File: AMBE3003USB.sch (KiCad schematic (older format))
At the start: 18 parts, among them P1 USB_B, U1 FT232RL, U2 TPS78319, U3 LD1117S33TR

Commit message: Add AMBE3003 chip to schematic
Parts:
- added C10, C9: 24p, symbol C
- added JP?: JUMPER, symbol JUMPER
- added U?: AMBE3003, symbol AMBE3003
- added Y1: 29.4912, symbol Crystal
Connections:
- wire segments 60 -> 117
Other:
- moved on the sheet: C1, C2, C3, C4, C5, C6, C7, C8, R1, R2, R3, U1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

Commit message: Add jumpers for AMBE3003 and some refactoring
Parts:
- removed JP?: JUMPER, symbol JUMPER
- added P2: CONN_02X16, symbol CONN_02X16
- added R10, R11, R12, R13, R14, R15, R16, R17, R18, R19, R4, R5, R6, R7, R8, R9: 3k3, symbol R
- gave numbers to parts that had none: 1
- renumbered U1 to U2, U2 to U3, U3 to U4
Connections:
- wire segments 117 -> 195
- no-connect marks 13 -> 40
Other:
- moved on the sheet: C1, C10, C2, C3, C4, C9, R3, U1

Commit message: Add Rs and Cs to USB connection
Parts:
- added C11, C12: 47p, symbol C
- added R20, R21: 27, symbol R
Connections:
- wire segments 195 -> 203
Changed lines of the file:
@@
 L USB_B P1
 U 1 1 591BECF9
-P 6200 4450
-F 0 "P1" H 6400 4250 50  0000 C CNN
-F 1 "USB_B" H 6150 4650 50  0000 C CNN
-F 2 "" V 6150 4350 50  0001 C CNN
-F 3 "" V 6150 4350 50  0000 C CNN
-	1    6200 4450
+P 5850 4450
+F 0 "P1" H 6050 4250 50  0000 C CNN
+F 1 "USB_B" H 5800 4650 50  0000 C CNN
+F 2 "" V 5800 4350 50  0001 C CNN
+F 3 "" V 5800 4350 50  0000 C CNN
+	1    5850 4450
 	0    -1   1    0
 $EndComp
@@
 L GND #PWR02
 U 1 1 591BEEC2
-P 6550 5000
-F 0 "#PWR02" H 6550 4750 50  0001 C CNN
-F 1 "GND" H 6550 4850 50  0000 C CNN
-F 2 "" H 6550 5000 50  0000 C CNN
-F 3 "" H 6550 5000 50  0000 C CNN
-	1    6550 5000
+P 6700 4950
+F 0 "#PWR02" H 6700 4700 50  0001 C CNN
+F 1 "GND" H 6700 4800 50  0000 C CNN
+F 2 "" H 6700 4950 50  0000 C CNN
+F 3 "" H 6700 4950 50  0000 C CNN
+	1    6700 4950
 	1    0    0    -1
 $EndComp
@@
 	6700 4000 6700 4600
 Wire Wire Line
-	6500 4250 6700 4250
+	6150 4250 6700 4250
 Connection ~ 6700 4250
 Wire Wire Line
-	6100 4900 6700 4900
-Wire Wire Line
-	6500 4550 6550 4550
-Wire Wire Line
-	6550 4550 6550 5000
-Connection ~ 6550 4900
+	6150 4550 6200 4550
 Wire Wire Line
 	10100 4850 10100 4700
@@
 	9800 3900 9250 3900
 Wire Wire Line
-	7200 4350 6500 4350
-Wire Wire Line
-	7300 4450 6500 4450
-Wire Wire Line
-	6100 4750 6100 4900
+	5750 4750 5750 4950
 Wire Wire Line
 	7350 3300 7600 3300
@@
 NoConn ~ 4700 6500
 NoConn ~ 4700 6400
+$Comp
+L R R20
+U 1 1 591D8344
+P 6900 4350
+F 0 "R20" V 6980 4350 50  0000 C CNN
+F 1 "27" V 6900 4350 50  0000 C CNN
+F 2 "" V 6830 4350 50  0000 C CNN
+F 3 "" H 6900 4350 50  0000 C CNN
+	1    6900 4350
+	0    1    1    0
+$EndComp
+$Comp
+L R R21
+U 1 1 591D83EB
+P 6900 4450
+F 0 "R21" V 6980 4450 50  0000 C CNN
+F 1 "27" V 6900 4450 50  0000 C CNN
+F 2 "" V 6830 4450 50  0000 C CNN
+F 3 "" H 6900 4450 50  0000 C CNN
+	1    6900 4450
+	0    1    1    0
+$EndComp
+Wire Wire Line
+	7200 4350 7050 4350
+Wire Wire Line
+	6150 4350 6750 4350
+Wire Wire Line
+	6150 4450 6750 4450
+Wire Wire Line
+	7050 4450 7300 4450
+$Comp
+L C C11
+U 1 1 591D9B45
+P 6350 4700
+F 0 "C11" H 6375 4800 50  0000 L CNN
+F 1 "47p" H 6375 4600 50  0000 L CNN
+F 2 "" H 6388 4550 50  0000 C CNN
+F 3 "" H 6350 4700 50  0000 C CNN
+	1    6350 4700
+	1    0    0    -1
+$EndComp
+Wire Wire Line
+	6700 4950 6700 4900
+Wire Wire Line
+	6200 4550 6200 4800
+Wire Wire Line
+	6200 4800 5750 4800
+Connection ~ 5750 4800
+$Comp
+L GND #PWR?
+U 1 1 591DA437
+P 5750 4950
+F 0 "#PWR?" H 5750 4700 50  0001 C CNN
+F 1 "GND" H 5750 4800 50  0000 C CNN
+F 2 "" H 5750 4950 50  0000 C CNN
+F 3 "" H 5750 4950 50  0000 C CNN
+	1    5750 4950
+	1    0    0    -1
+$EndComp
+$Comp
+L GND #PWR?
+U 1 1 591DA49F
+P 6350 4950
+F 0 "#PWR?" H 6350 4700 50  0001 C CNN
+F 1 "GND" H 6350 4800 50  0000 C CNN
+F 2 "" H 6350 4950 50  0000 C CNN
+F 3 "" H 6350 4950 50  0000 C CNN
+	1    6350 4950
+	1    0    0    -1
+$EndComp
+Wire Wire Line
+	6350 4950 6350 4850
+Wire Wire Line
+	6350 4550 6350 4450
+Connection ~ 6350 4450
+$Comp
+L C C12
+U 1 1 591DAD3E
+P 6500 3800
+F 0 "C12" H 6525 3900 50  0000 L CNN
+F 1 "47p" H 6525 3700 50  0000 L CNN
+F 2 "" H 6538 3650 50  0000 C CNN
+F 3 "" H 6500 3800 50  0000 C CNN
+	1    6500 3800
+	1    0    0    -1
+$EndComp
+$Comp
+L GND #PWR?
+U 1 1 591DAE26
+P 6500 4050
+F 0 "#PWR?" H 6500 3800 50  0001 C CNN
+F 1 "GND" H 6500 3900 50  0000 C CNN
+F 2 "" H 6500 4050 50  0000 C CNN
+F 3 "" H 6500 4050 50  0000 C CNN
+	1    6500 4050
+	1    0    0    -1
+$EndComp
+Wire Wire Line
+	6500 3650 6350 3650
+Wire Wire Line
+	6350 3650 6350 4250
+Connection ~ 6350 4250
+Wire Wire Line
+	6500 4050 6500 3950
 $EndSCHEMATC

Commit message: Refactor USB connection and drop 3v3 regulator
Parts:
- removed C10: 24p, symbol C
- removed C7: 100n, symbol C
- removed C8: 10µ, symbol CP
- removed U4: LD1117S33TR, SOT-223, symbol LD1117S33TR
- removed Y1: 29.4912, symbol Crystal
- added C10, C13: 1µ, symbol CP
- added C?: 1µ, symbol C
- added L1: L_Small, symbol L_Small
- added R22: 5k1, symbol R
- added R?: 10, symbol R
- added R?: 24k, symbol R
- added X1: TCXO3, symbol TCXO3
- C9: value 24p -> 10n
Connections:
- wire segments 203 -> 220
- no-connect marks 40 -> 37
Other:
- moved on the sheet: C5

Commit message: Add reset circuit
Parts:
- added C14, C7: 10n, symbol C
- added R23: 5.1, symbol R
- added R24, R27: 24k, symbol R
- added R28: 3k74, symbol R
- added R29: 10k, symbol R
- added U4: TPS3805, SOT-23-5, symbol TPS3805
- R22: value 5k1 -> 5.1
- gave numbers to parts that had none: 3
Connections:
- net labels added: +3V3
- wire segments 220 -> 246
- no-connect marks 37 -> 35

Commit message: Added support for AMBE3000; Added 3v3 Regulator; Added Codec Connections
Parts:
- added C10, C11, C12, C13, C14, C15, C4, C5, C6, C7, C8, C9: 100n, symbol C
- added C2, C3: 10u, symbol C
- added C? (x2): 10u, symbol CP
- added J1: McBSP, symbol CONN_02X04
- added J2: CODEC_SPI_I2C, symbol CONN_02X06
- added J?: ACONF, symbol CONN_02X03
- added R19, R20, R21, R22, R23, R24, R25, R26, R27, R28, R29, R? (x3): 0R, symbol R
- added R? (x3): 3k3, symbol R
- added R?: 10k, symbol R
- added TP1, TP2, TP3: TEST, symbol TEST
- added U?: LD1117S33TR, TO_SOT_Packages_SMD:SOT-223, symbol LD1117S33TR
- D1: renamed from D3; symbol LED -> LED-RESCUE-AMBE3003USB
- D2: renamed from D1; symbol LED -> LED-RESCUE-AMBE3003USB
- D3: renamed from D2; symbol LED -> LED-RESCUE-AMBE3003USB
- P2: renamed from P1; symbol USB_B -> USB_B-RESCUE-AMBE3003USB
- X1: symbol TCXO3 -> TCXO3-RESCUE-AMBE3003USB
- renumbered C7 to C1, C1 to C16, C9 to C17, C2 to C18, C11 to C19, C12 to C20, C3 to C21, C4 to C22, C10 to C23, C14 to C24, C5 to C25, C13 to C26, C8 to C27, C6 to C28, P2 to P1, R23 to R1, R4 to R10, R5 to R11, R6 to R12, R7 to R13, R8 to R14, R9 to R15, R10 to R16, R11 to R17, R24 to R18, R12 to R2, R13 to R3, R22 to R30, R3 to R31, R20 to R32, R21 to R33, R28 to R34, R29 to R35, R25 to R36, R26 to R37, R27 to R38, R1 to R39, R14 to R4, R2 to R40, R15 to R5, R16 to R6, R17 to R7, R18 to R8, R19 to R9, U4 to U2, U2 to U3, U3 to U4
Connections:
- net labels added: AMBE_RESETn, CODEC_RESETn, PWREN, UART_RTS, UART_RX, UART_TX
- wire segments 246 -> 357
- no-connect marks 35 -> 15
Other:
- moved on the sheet: C16, C17, C18, C19, C20, C21, C22, C23, C24, C25, C26, C27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

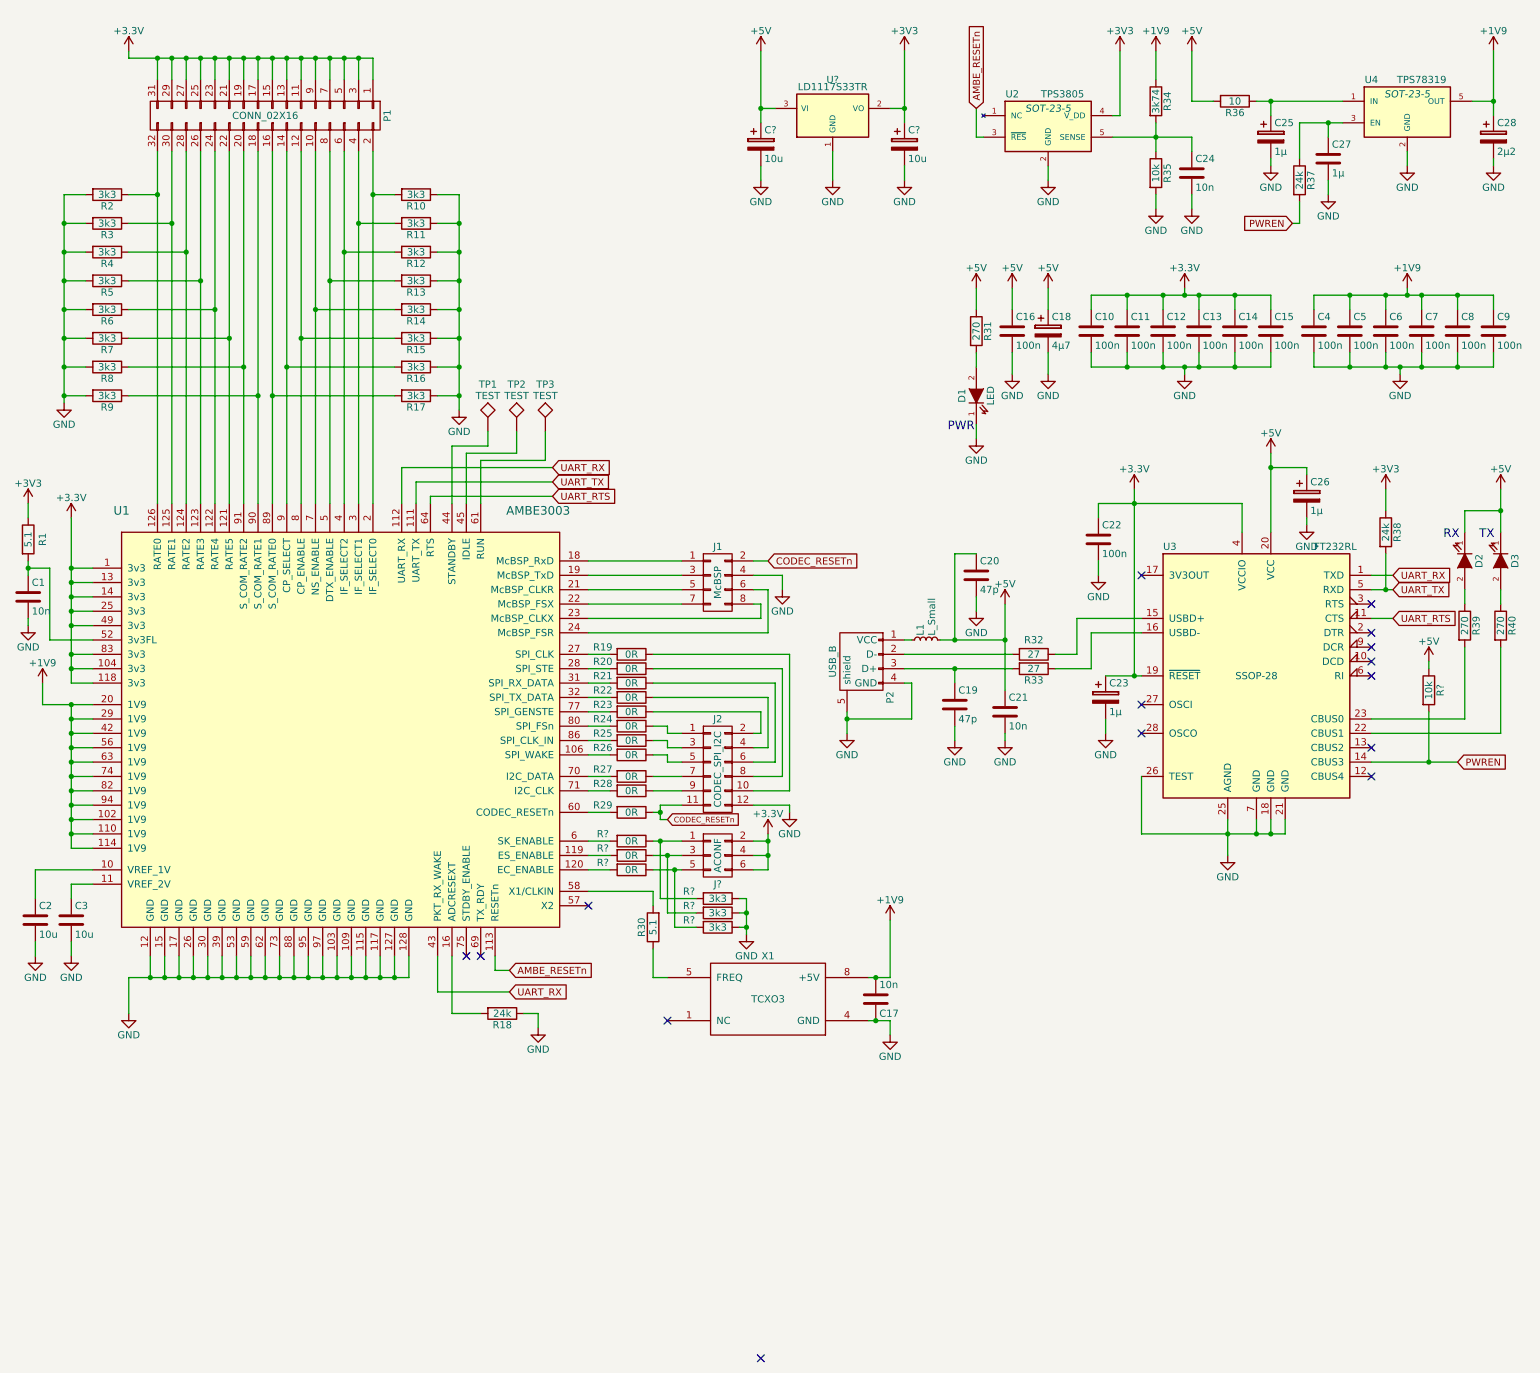
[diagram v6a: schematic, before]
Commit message: Annotate PCB
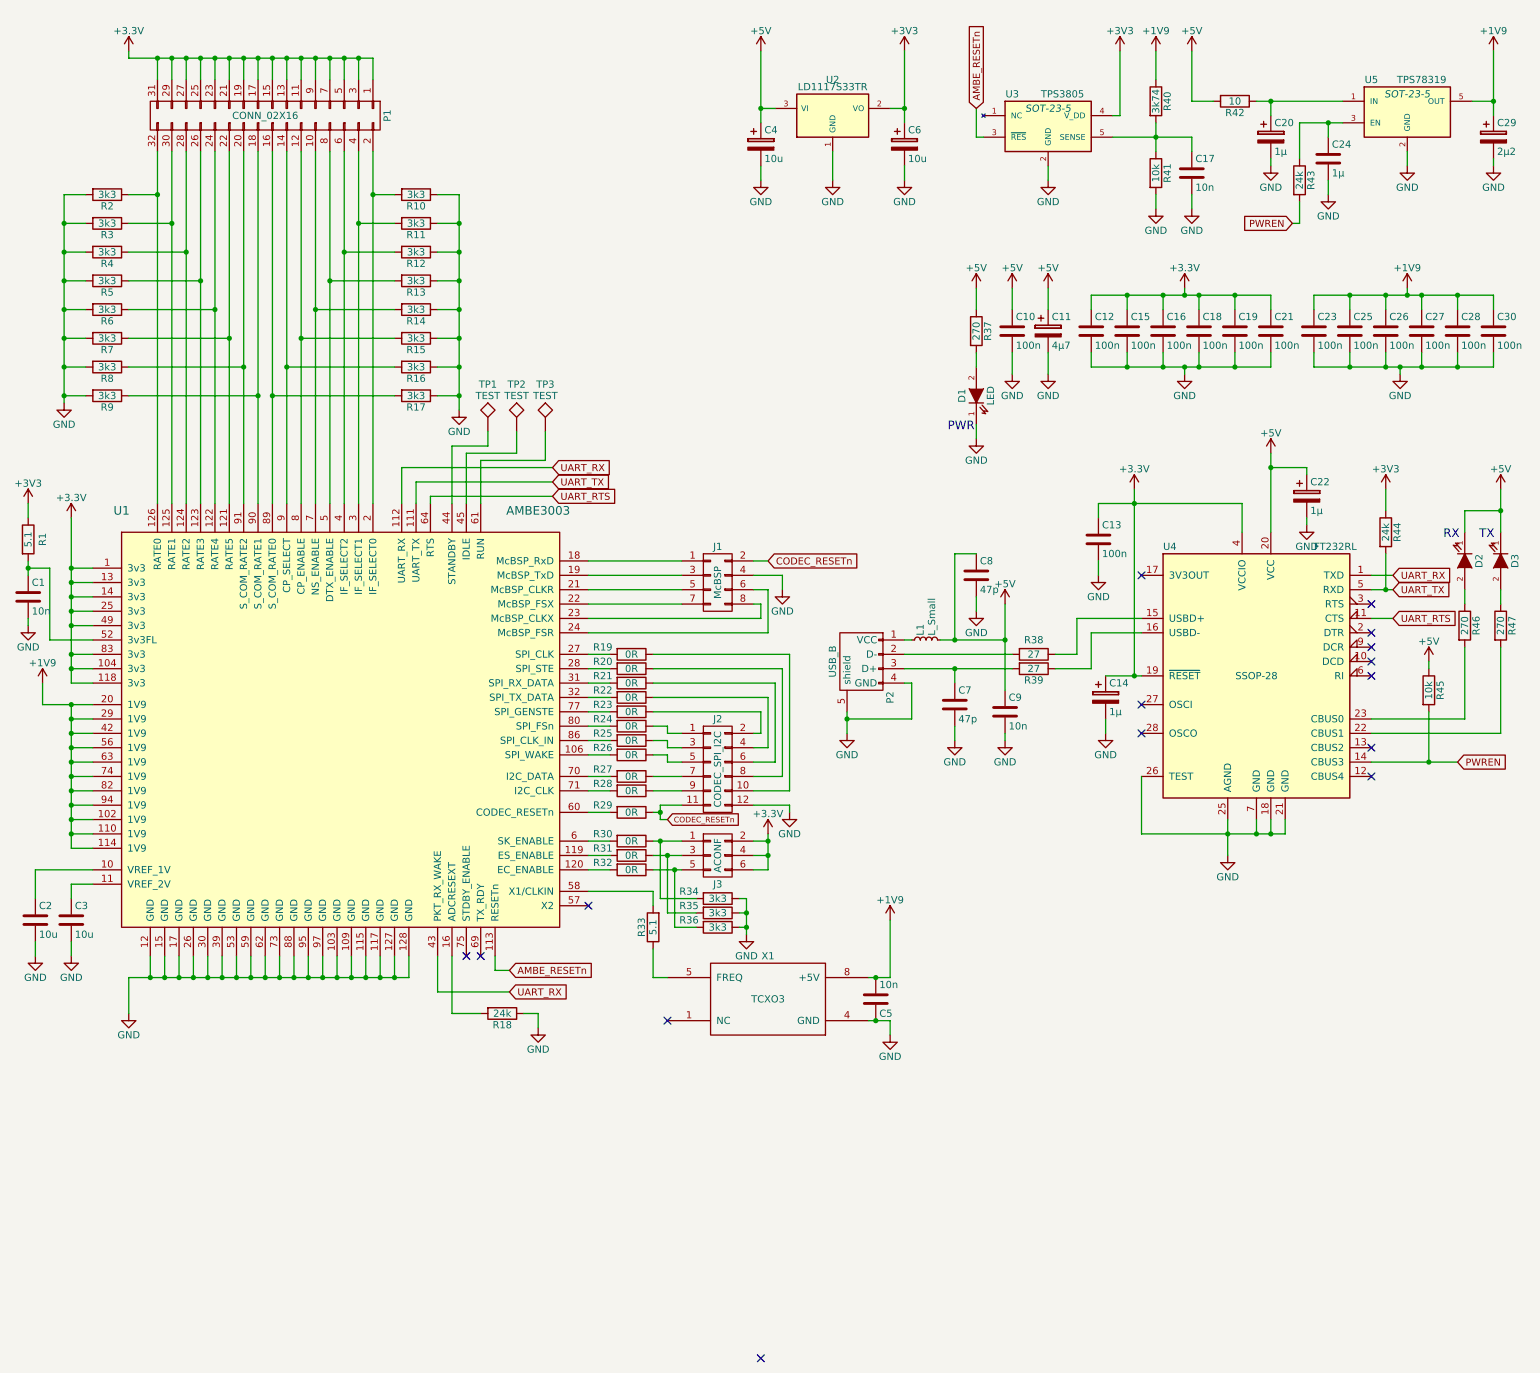
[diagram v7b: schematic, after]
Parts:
- gave numbers to parts that had none: 11
- renumbered C16 to C10, C18 to C11, C10 to C12, C22 to C13, C23 to C14, C11 to C15, C12 to C16, C24 to C17, C13 to C18, C14 to C19, C25 to C20, C15 to C21, C26 to C22, C4 to C23, C27 to C24, C5 to C25, C6 to C26, C7 to C27, C8 to C28, C28 to C29, C9 to C30, C17 to C5, C19 to C7, C20 to C8, C21 to C9, R30 to R33, R31 to R37, R32 to R38, R33 to R39, R34 to R40, R35 to R41, R36 to R42, R37 to R43, R38 to R44, R39 to R46, R40 to R47, U2 to U3, U3 to U4, U4 to U5

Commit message: Refactoring and re-configured some pins
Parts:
- TP1, TP2, TP3: symbol TEST -> TEST-RESCUE-AMBE3003USB
- U3, U5: footprint SOT-23-5 -> (none)
